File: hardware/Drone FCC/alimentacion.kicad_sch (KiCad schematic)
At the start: 14 parts, among them J19 PM02 PixHawk, U3 ZLDO1117QG33TA

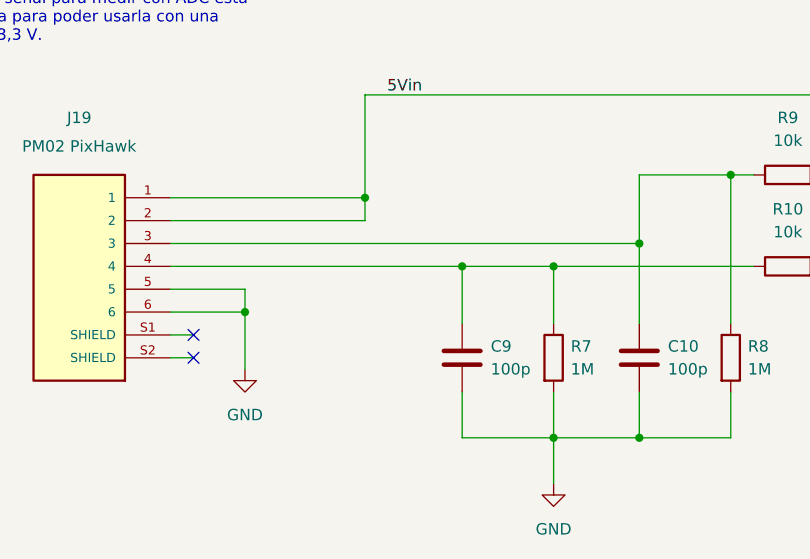
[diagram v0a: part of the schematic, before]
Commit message: moved NRST cap near mcu pin, changed v meas adc pin
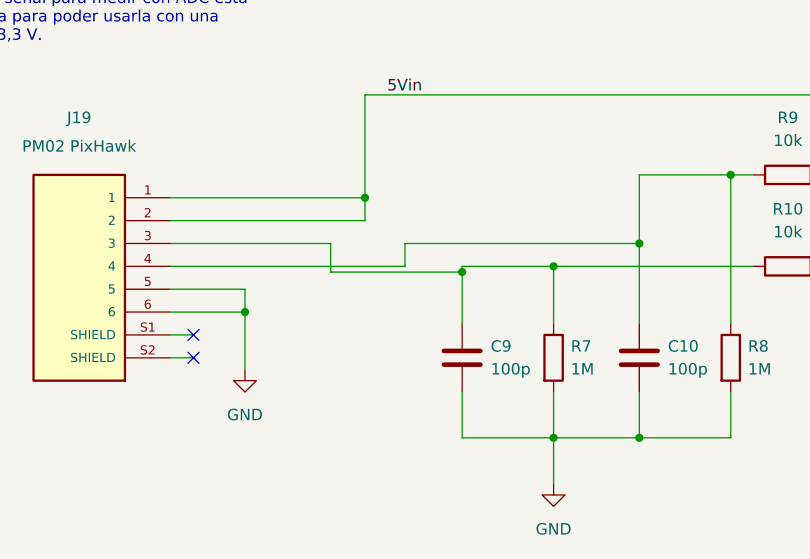
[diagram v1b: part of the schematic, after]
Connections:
- net at C9.1, R10.1, R7.1: now also J19.3; no longer J19.4
- net at C10.1, R8.1, R9.1: now also J19.4; no longer J19.3
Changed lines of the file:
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@@
   (junction (at 154.305 66.04) (diameter 0) (color 0 0 0 0)
   )
+  (junction (at 90.805 101.6) (diameter 0) (color 0 0 0 0)
+  )
   (junction (at 110.49 120.015) (diameter 0) (color 0 0 0 0)
   )
@@
   )
   (junction (at 165.735 66.04) (diameter 0) (color 0 0 0 0)
-  )
-  (junction (at 90.805 100.965) (diameter 0) (color 0 0 0 0)
   )
   (junction (at 120.65 90.805) (diameter 0) (color 0 0 0 0)
@@
     (stroke (width 0) (type default) (color 0 0 0 0))
   )
+  (wire (pts (xy 90.805 101.6) (xy 90.805 107.315))
+    (stroke (width 0) (type default) (color 0 0 0 0))
+  )
+  (wire (pts (xy 76.2 101.6) (xy 90.805 101.6))
+    (stroke (width 0) (type default) (color 0 0 0 0))
+  )
   (wire (pts (xy 187.325 77.47) (xy 201.295 77.47))
     (stroke (width 0) (type default) (color 0 0 0 0))
@@
     (stroke (width 0) (type default) (color 0 0 0 0))
   )
-  (wire (pts (xy 58.42 100.965) (xy 90.805 100.965))
-    (stroke (width 0) (type default) (color 0 0 0 0))
-  )
   (wire (pts (xy 201.295 66.04) (xy 194.945 66.04))
     (stroke (width 0) (type default) (color 0 0 0 0))
@@
     (stroke (width 0) (type default) (color 0 0 0 0))
   )
+  (wire (pts (xy 76.2 98.425) (xy 76.2 101.6))
+    (stroke (width 0) (type default) (color 0 0 0 0))
+  )
   (wire (pts (xy 80.01 93.345) (xy 80.01 95.885))
     (stroke (width 0) (type default) (color 0 0 0 0))
@@
     (stroke (width 0) (type default) (color 0 0 0 0))
   )
-  (wire (pts (xy 58.42 98.425) (xy 110.49 98.425))
+  (wire (pts (xy 84.455 98.425) (xy 110.49 98.425))
     (stroke (width 0) (type default) (color 0 0 0 0))
   )
@@
     (stroke (width 0) (type default) (color 0 0 0 0))
   )
+  (wire (pts (xy 58.42 100.965) (xy 84.455 100.965))
+    (stroke (width 0) (type default) (color 0 0 0 0))
+  )
   (wire (pts (xy 120.65 90.805) (xy 123.19 90.805))
     (stroke (width 0) (type default) (color 0 0 0 0))
   )
-  (wire (pts (xy 90.805 100.965) (xy 90.805 107.315))
+  (wire (pts (xy 90.805 100.965) (xy 90.805 101.6))
     (stroke (width 0) (type default) (color 0 0 0 0))
   )
@@
     (stroke (width 0) (type default) (color 0 0 0 0))
   )
+  (wire (pts (xy 58.42 98.425) (xy 76.2 98.425))
+    (stroke (width 0) (type default) (color 0 0 0 0))
+  )
   (wire (pts (xy 165.735 77.47) (xy 173.355 77.47))
     (stroke (width 0) (type default) (color 0 0 0 0))
   )
+  (wire (pts (xy 84.455 100.965) (xy 84.455 98.425))
+    (stroke (width 0) (type default) (color 0 0 0 0))
+  )

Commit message: add PWR_FLAGs to schematic
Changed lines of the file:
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@@
   (junction (at 201.295 66.04) (diameter 0) (color 0 0 0 0)
   )
+  (junction (at 213.995 77.47) (diameter 0) (color 0 0 0 0)
+  )
   (junction (at 187.325 77.47) (diameter 0) (color 0 0 0 0)
   )
   (junction (at 154.305 66.04) (diameter 0) (color 0 0 0 0)
   )
+  (junction (at 165.735 57.15) (diameter 0) (color 0 0 0 0)
+  )
   (junction (at 90.805 101.6) (diameter 0) (color 0 0 0 0)
   )
@@
   )
   (junction (at 165.735 66.04) (diameter 0) (color 0 0 0 0)
+  )
+  (junction (at 120.65 55.88) (diameter 0) (color 0 0 0 0)
+  )
+  (junction (at 80.01 81.915) (diameter 0) (color 0 0 0 0)
   )
   (junction (at 120.65 90.805) (diameter 0) (color 0 0 0 0)
@@
     (stroke (width 0) (type default) (color 0 0 0 0))
   )
+  (wire (pts (xy 80.01 81.915) (xy 80.01 93.345))
+    (stroke (width 0) (type default) (color 0 0 0 0))
+  )
   (wire (pts (xy 201.295 66.04) (xy 213.995 66.04))
     (stroke (width 0) (type default) (color 0 0 0 0))
@@
     (stroke (width 0) (type default) (color 0 0 0 0))
   )
+  (wire (pts (xy 165.735 55.245) (xy 165.735 57.15))
+    (stroke (width 0) (type default) (color 0 0 0 0))
+  )
   (polyline (pts (xy 210.185 80.645) (xy 220.98 80.645))
     (stroke (width 0) (type default) (color 0 0 0 0))
@@
     (stroke (width 0) (type default) (color 0 0 0 0))
   )
+  (wire (pts (xy 120.65 55.88) (xy 140.97 55.88))
+    (stroke (width 0) (type default) (color 0 0 0 0))
+  )
   (wire (pts (xy 110.49 90.805) (xy 110.49 98.425))
     (stroke (width 0) (type default) (color 0 0 0 0))
   )
-  (wire (pts (xy 80.01 81.915) (xy 80.01 93.345))
-    (stroke (width 0) (type default) (color 0 0 0 0))
-  )
   (wire (pts (xy 58.42 100.965) (xy 84.455 100.965))
     (stroke (width 0) (type default) (color 0 0 0 0))
@@
     (stroke (width 0) (type default) (color 0 0 0 0))
   )
+  (wire (pts (xy 213.995 66.04) (xy 234.315 66.04))
+    (stroke (width 0) (type default) (color 0 0 0 0))
+  )
   (wire (pts (xy 90.805 100.965) (xy 90.805 101.6))
     (stroke (width 0) (type default) (color 0 0 0 0))
   )
+  (wire (pts (xy 235.585 75.565) (xy 235.585 77.47))
+    (stroke (width 0) (type default) (color 0 0 0 0))
+  )
   (wire (pts (xy 90.805 100.965) (xy 100.965 100.965))
     (stroke (width 0) (type default) (color 0 0 0 0))
@@
     (stroke (width 0) (type default) (color 0 0 0 0))
   )
+  (wire (pts (xy 120.65 53.975) (xy 120.65 55.88))
+    (stroke (width 0) (type default) (color 0 0 0 0))
+  )
   (wire (pts (xy 179.705 66.04) (xy 173.355 66.04))
     (stroke (width 0) (type default) (color 0 0 0 0))
@@
     (stroke (width 0) (type default) (color 0 0 0 0))
   )
-  (wire (pts (xy 213.995 66.04) (xy 234.315 66.04))
+  (wire (pts (xy 213.995 77.47) (xy 235.585 77.47))
     (stroke (width 0) (type default) (color 0 0 0 0))
   )
@@
     (stroke (width 0) (type default) (color 0 0 0 0))
   )
-  (wire (pts (xy 118.11 55.88) (xy 140.97 55.88))
+  (wire (pts (xy 118.11 55.88) (xy 120.65 55.88))
     (stroke (width 0) (type default) (color 0 0 0 0))
   )
   (wire (pts (xy 165.735 66.04) (xy 173.355 66.04))
+    (stroke (width 0) (type default) (color 0 0 0 0))
+  )
+  (wire (pts (xy 80.01 79.375) (xy 80.01 81.915))
     (stroke (width 0) (type default) (color 0 0 0 0))
   )
@@
     (pin "3")
   )
+  (symbol (lib_id "power:PWR_FLAG") (at 235.585 75.565 0) (unit 1)
+    (in_bom yes) (on_board yes)
+    (property "Reference" "#FLG?" (id 0) (at 235.585 73.66 0)
+      (effects (font (size 1.27 1.27)) hide)
+    )
+    (property "Value" "PWR_FLAG" (id 1) (at 235.585 71.755 0))
+    (property "Footprint" "" (id 2) (at 235.585 75.565 0)
+      (effects (font (size 1.27 1.27)) hide)
+    )
+    (property "Datasheet" "~" (id 3) (at 235.585 75.565 0)
+      (effects (font (size 1.27 1.27)) hide)
+    )
+    (pin "1")
+  )
+  (symbol (lib_id "power:PWR_FLAG") (at 120.65 53.975 0) (unit 1)
+    (in_bom yes) (on_board yes) (fields_autoplaced)
+    (property "Reference" "#FLG0103" (id 0) (at 120.65 52.07 0)
+      (effects (font (size 1.27 1.27)) hide)
+    )
+    (property "Value" "PWR_FLAG" (id 1) (at 120.65 48.26 0))
+    (property "Footprint" "" (id 2) (at 120.65 53.975 0)
+      (effects (font (size 1.27 1.27)) hide)
+    )
+    (property "Datasheet" "~" (id 3) (at 120.65 53.975 0)
+      (effects (font (size 1.27 1.27)) hide)
+    )
+    (pin "1")
+  )
   (symbol (lib_id "Device:C") (at 173.355 71.755 0) (mirror y) (unit 1)
     (in_bom yes) (on_board yes) (fields_autoplaced)
@@
     (pin "2")
   )
+  (symbol (lib_id "power:PWR_FLAG") (at 80.01 79.375 0) (unit 1)
+    (in_bom yes) (on_board yes) (fields_autoplaced)
+    (property "Reference" "#FLG0102" (id 0) (at 80.01 77.47 0)
+      (effects (font (size 1.27 1.27)) hide)
+    )
+    (property "Value" "PWR_FLAG" (id 1) (at 80.01 73.66 0))
+    (property "Footprint" "" (id 2) (at 80.01 79.375 0)
+      (effects (font (size 1.27 1.27)) hide)
+    )
+    (property "Datasheet" "~" (id 3) (at 80.01 79.375 0)
+      (effects (font (size 1.27 1.27)) hide)
+    )
+    (pin "1")
+  )
   (symbol (lib_id "Device:C") (at 165.735 71.755 0) (mirror x) (unit 1)
     (in_bom yes) (on_board yes) (fields_autoplaced)
@@
     (pin "2")
   )
+  (symbol (lib_id "power:PWR_FLAG") (at 165.735 55.245 0) (unit 1)
+    (in_bom yes) (on_board yes) (fields_autoplaced)
+    (property "Reference" "#FLG0101" (id 0) (at 165.735 53.34 0)
+      (effects (font (size 1.27 1.27)) hide)
+    )
+    (property "Value" "PWR_FLAG" (id 1) (at 165.735 49.53 0))
+    (property "Footprint" "" (id 2) (at 165.735 55.245 0)
+      (effects (font (size 1.27 1.27)) hide)
+    )
+    (property "Datasheet" "~" (id 3) (at 165.735 55.245 0)
+      (effects (font (size 1.27 1.27)) hide)
+    )
+    (pin "1")
+  )
   (symbol (lib_id "Device:C") (at 110.49 111.125 0) (unit 1)
